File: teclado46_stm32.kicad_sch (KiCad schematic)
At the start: 15 parts, among them J2 78171-0004, Q1 DTC123J, SW1 Reset_SW, U1 XC6206PxxxMR, U2 STM32G0B1RETx

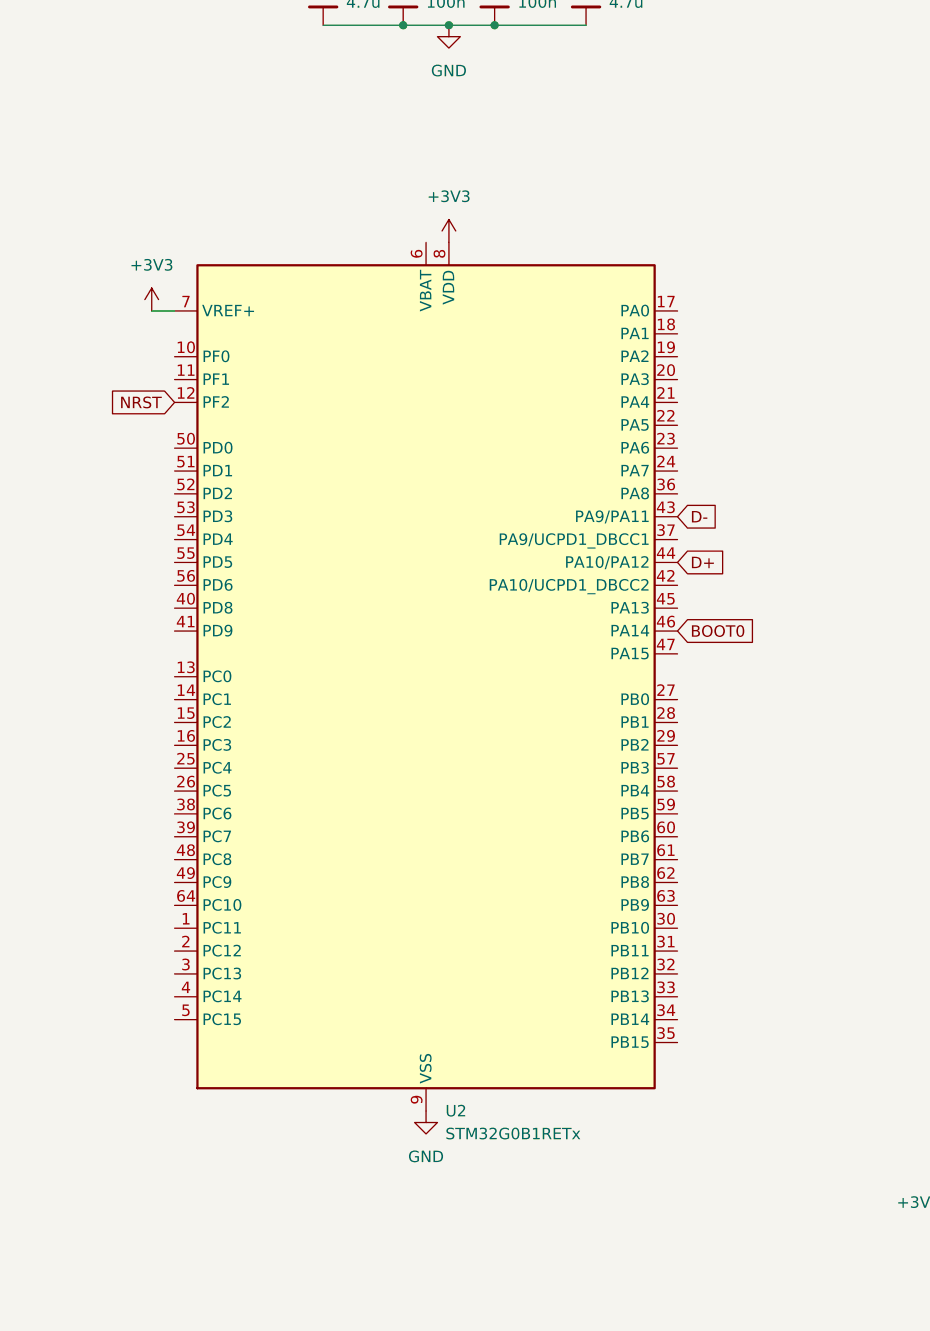
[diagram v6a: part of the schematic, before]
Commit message: chore: switch to g0b1cbt6
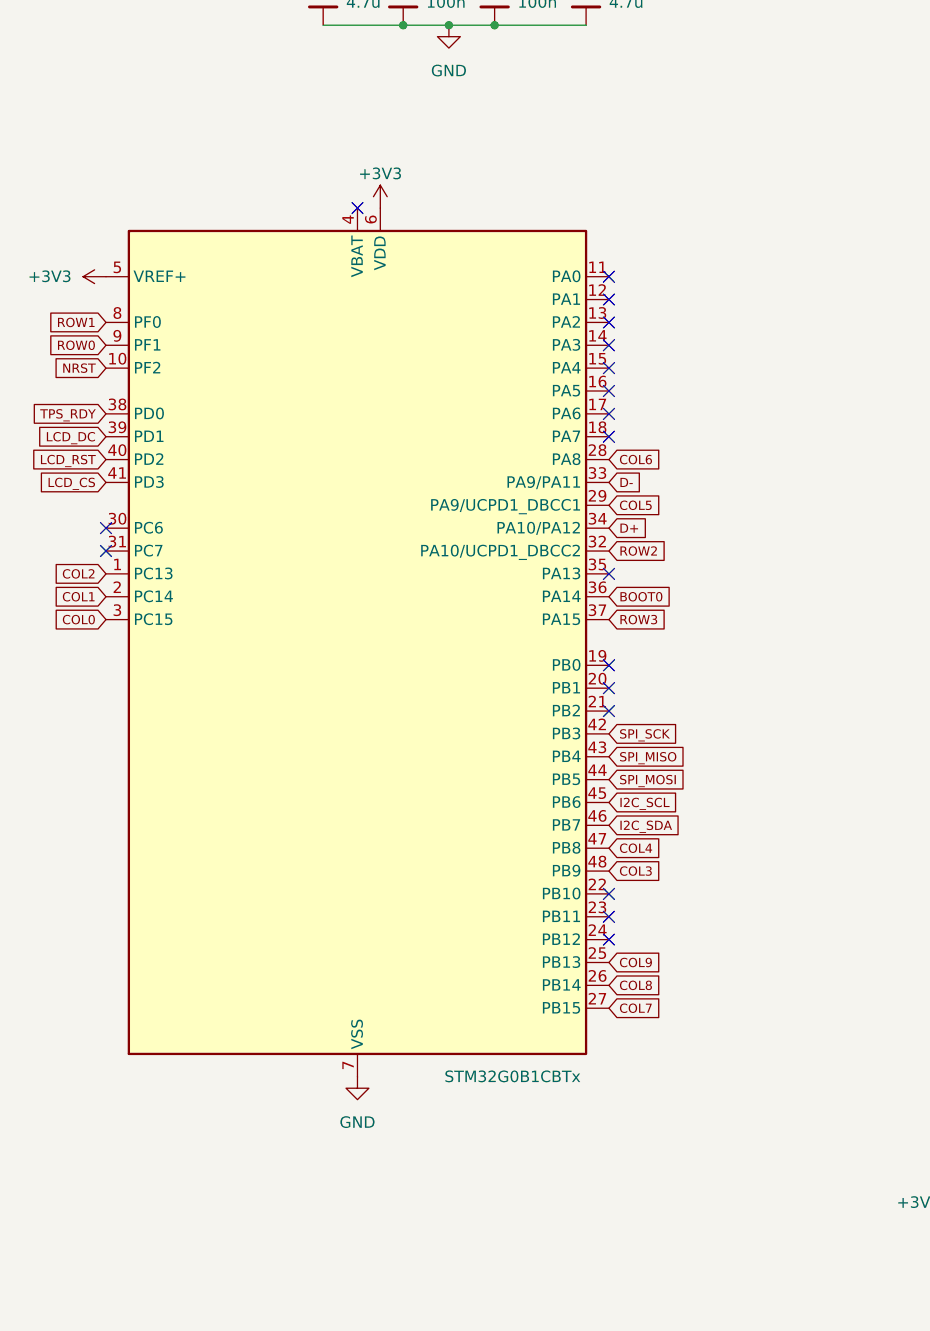
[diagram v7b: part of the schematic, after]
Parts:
- removed U2: STM32G0B1RETx, Package_QFP:LQFP-64_10x10mm_P0.5mm, symbol MCU_ST_STM32G0:STM32G0B1RETx
- added U4: STM32G0B1CBTx, Package_QFP:LQFP-48_7x7mm_P0.5mm, symbol MCU_ST_STM32G0:STM32G0B1CBTx
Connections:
- net +3V3: now also U4.5 (VREF+), U4.6 (VDD)
- net BOOT0: now also U4.36 (PA14)
- net D+: now also U4.34 (PA10/PA12)
- net D-: now also U4.33 (PA9/PA11)
- net GND: now also U4.7 (VSS)
- net NRST: now also U4.10 (PF2)
- new net COL0: U4.3 (PC15)
- new net COL1: U4.2 (PC14)
- new net COL2: U4.1 (PC13)
- new net COL3: U4.48 (PB9)
- new net COL4: U4.47 (PB8)
- new net COL5: U4.29 (PA9/UCPD1_DBCC1)
- new net COL6: U4.28 (PA8)
- new net COL7: U4.27 (PB15)
- new net COL8: U4.26 (PB14)
- new net COL9: U4.25 (PB13)
- new net I2C_SCL: U4.45 (PB6)
- new net I2C_SDA: U4.46 (PB7)
- new net LCD_CS: U4.41 (PD3)
- new net LCD_DC: U4.39 (PD1)
- new net LCD_RST: U4.40 (PD2)
- new net ROW0: U4.9 (PF1)
- new net ROW1: U4.8 (PF0)
- new net ROW2: U4.32 (PA10/UCPD1_DBCC2)
- new net ROW3: U4.37 (PA15)
- new net SPI_MISO: U4.43 (PB4)
- new net SPI_MOSI: U4.44 (PB5)
- new net SPI_SCK: U4.42 (PB3)
- new net TPS_RDY: U4.38 (PD0)
- no-connect marks 0 -> 18

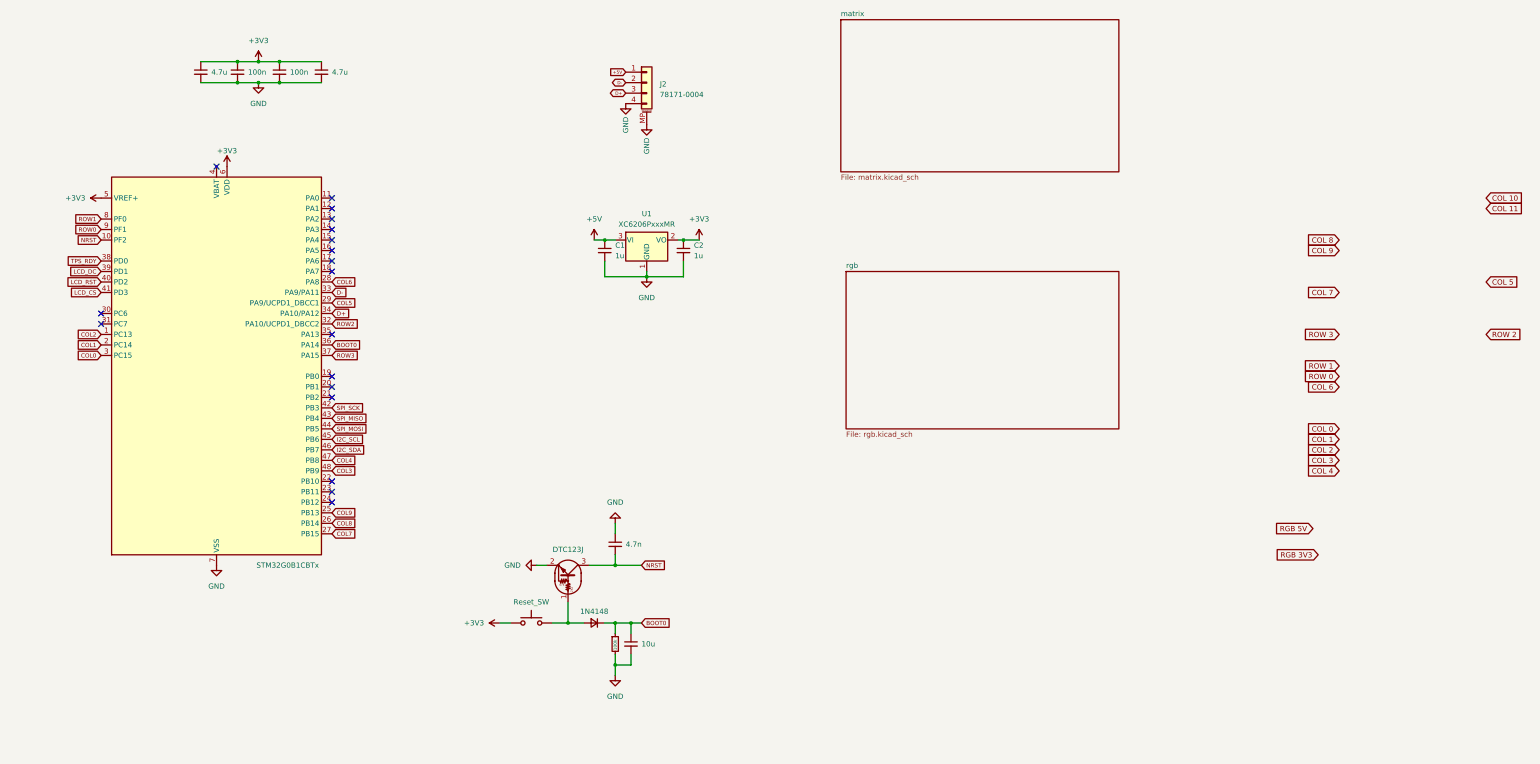
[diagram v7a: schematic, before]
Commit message: chore: open-drain for rgb
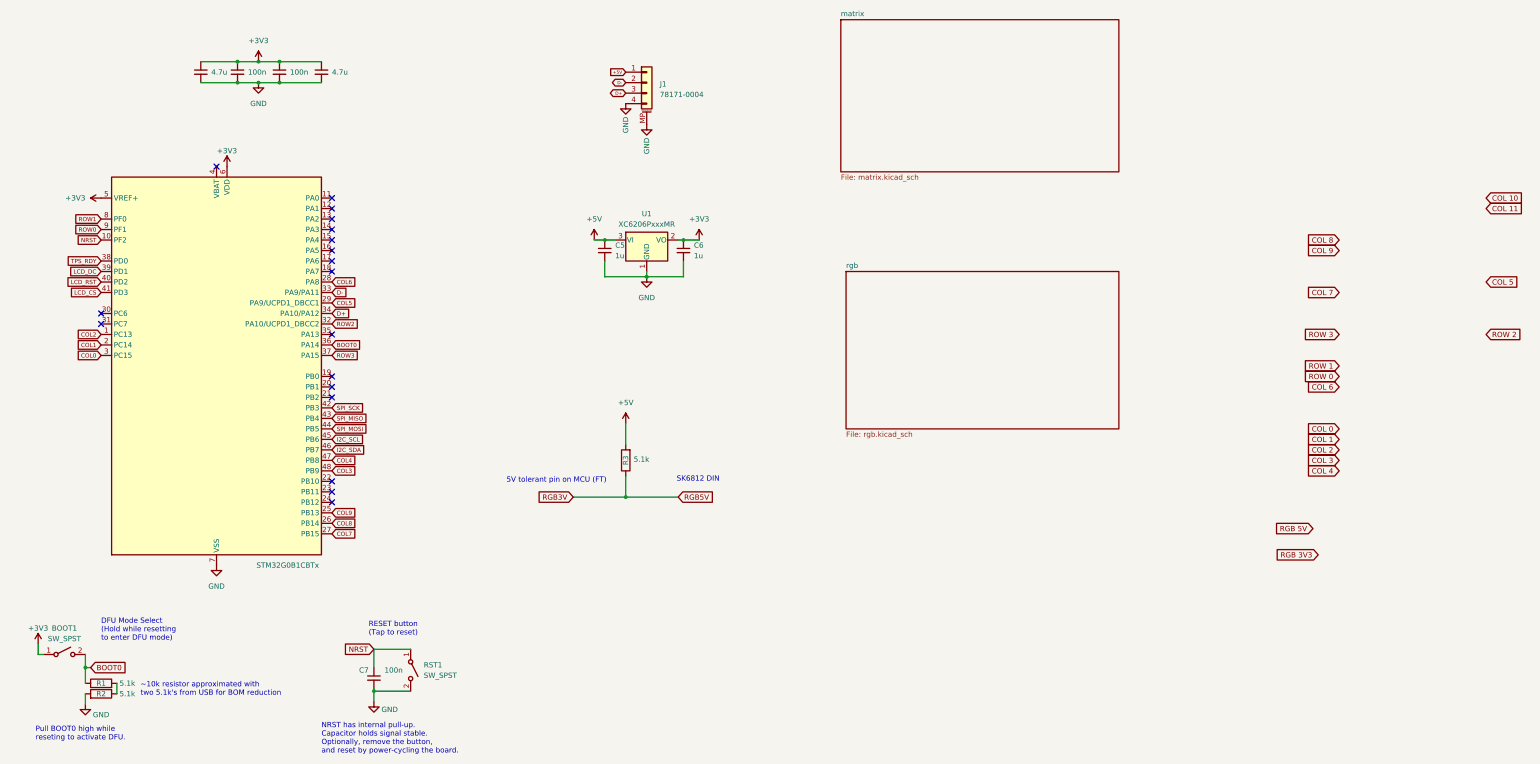
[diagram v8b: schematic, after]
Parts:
- removed C12: 4.7n, Capacitor_SMD:C_0805_2012Metric, symbol Device:C_Small
- removed C13: 10u, Capacitor_SMD:C_0805_2012Metric, symbol Device:C_Small
- removed D47: 1N4148, Diode_SMD:D_SOD-123, symbol Device:D_Small
- removed Q1: DTC123J, Package_TO_SOT_SMD:SOT-23, symbol Transistor_BJT:DTC123J
- removed R11: 100k, Resistor_SMD:R_0805_2012Metric, symbol Device:R_Small
- removed SW1: Reset_SW, PCM_marbastlib-various:SW_SPST_SKQG_WithStem, symbol Switch:SW_Push
- added BOOT1, RST1: SW_SPST, Button_Switch_SMD:SW_SPST_TL3342, symbol Switch:SW_SPST
- added C7: 100n, Capacitor_SMD:C_0402_1005Metric, symbol Device:C_Small
- added R1, R2, R3: 5.1k, Resistor_SMD:R_0402_1005Metric, symbol Device:R
- renumbered C18 to C1, C16 to C2, C14 to C3, C17 to C4, C1 to C5, C2 to C6, J2 to J1, U4 to U2
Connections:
- net +3V3: now also BOOT1.1 (A)
- net +5V: now also R3.2
- net BOOT0: now also BOOT1.2 (B), R1.1
- net GND: now also C7.2, R2.2, RST1.2 (B)
- net NRST: now also C7.1, RST1.1 (A)
- new net: R1.2, R2.1
- new net RGB3V: R3.1
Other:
- note added: "5V tolerant pin on MCU (FT)"
- note added: "DFU Mode Select (Hold while resetting to enter DFU mode)"
- note added: "NRST has internal pull-up. Capacitor holds signal stable. Optionally, remove the button, and reset by power-cycling the board."
- note added: "Pull BOOT0 high while reseting to activate DFU."
- note added: "RESET button (Tap to reset)"
- note added: "SK6812 DIN"
- note added: "~10k resistor approximated with two 5.1k's from USB for BOM reduction"
